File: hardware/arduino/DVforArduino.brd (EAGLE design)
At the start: 50 x 50 mm, 55 parts, among them Q1 2N7000, Q2 2N7000, U1 CML-MICRO_CMX589AE2, U2 CML-MICRO_CMX589AP4, U3 OPAMP-DUALDIP, Y1 4.9152MHz

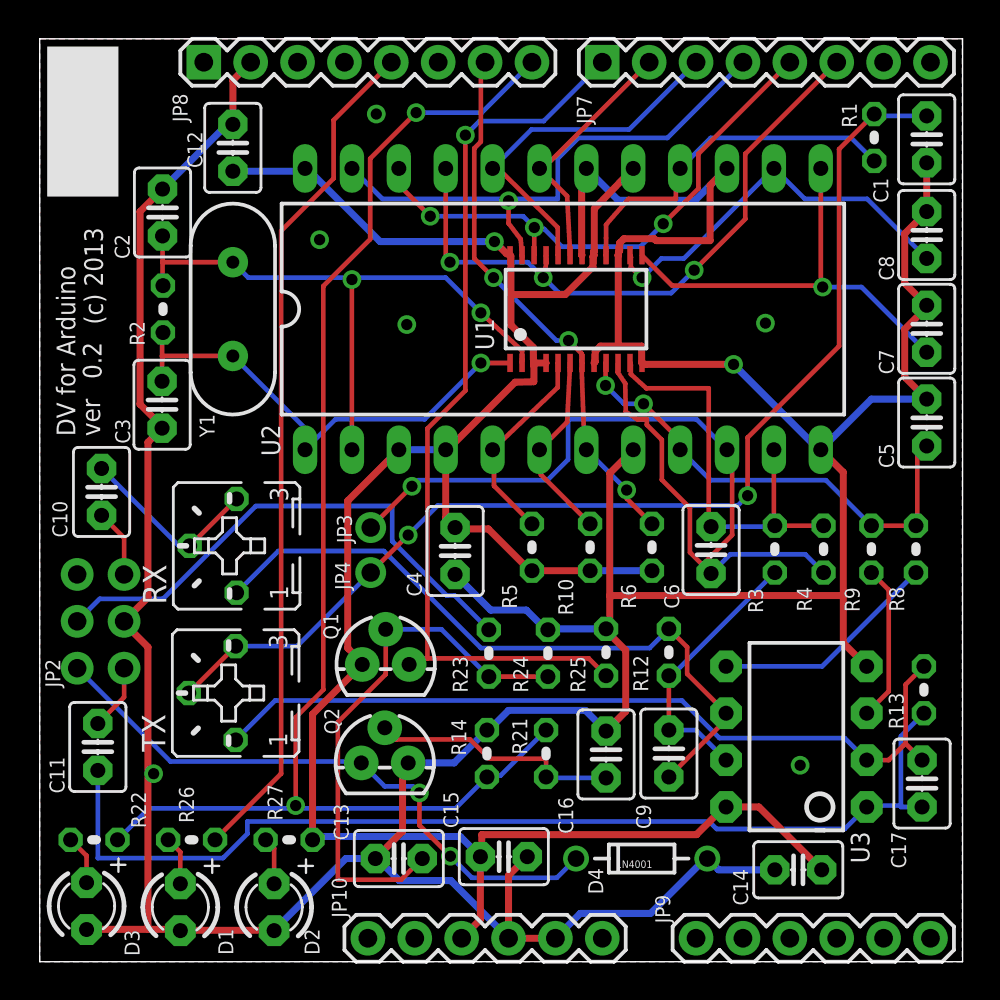
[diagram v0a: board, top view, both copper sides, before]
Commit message: 
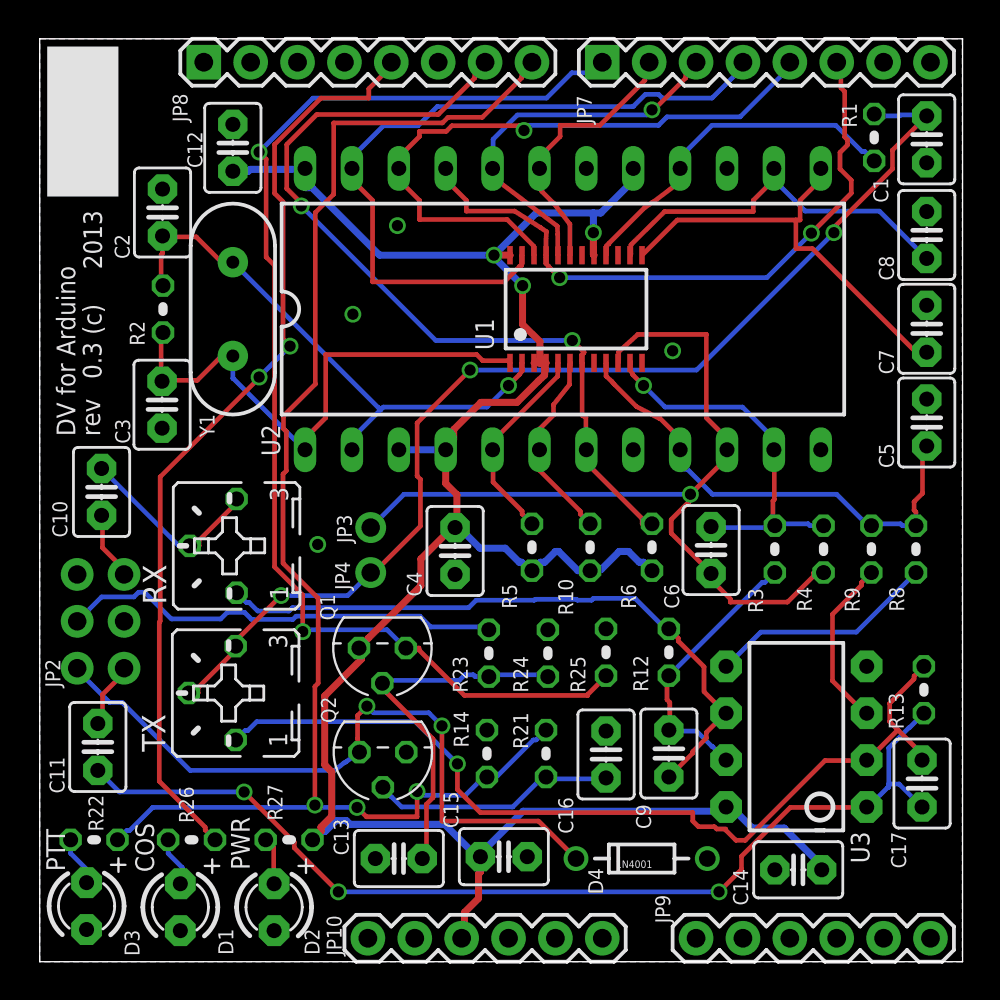
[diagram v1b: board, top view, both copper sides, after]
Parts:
- Q1, Q2: device SparkFun-DiscreteSemi:TO-92 -> transistor-fet:TO92
- moved Q1 0.91 mm to (18.6, 17.0), turned to 180 degrees
- moved Q2 0.59 mm to (18.6, 11.4), turned to 180 degrees
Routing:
- net GND: track 235.2 -> 0.00 mm, vias 7 -> 4
- net PLLACQ: track 29.6 -> 46.3 mm, vias 3 -> 2
- net COS: track 49.6 -> 66.1 mm, vias 1 -> 2
- net RX_SN: track 29.7 -> 40.1 mm, vias 1 -> 0
- net N$1: track 29.5 -> 20.1 mm
- net RADIO_PTT: track 33.2 -> 38.4 mm
- net PTT: track 73.5 -> 78.6 mm, vias 2 -> 3
- net TXCLK: track 30.2 -> 35.2 mm, vias 3 -> 1
- net RX_FB: track 52.0 -> 47.1 mm
- net COS_LED: track 46.1 -> 50.8 mm, vias 0 -> 2
- net RADIO_COS: track 28.8 -> 24.2 mm
- net N$28: track 44.7 -> 49.1 mm, vias 0 -> 1
- net XTAL: track 34.3 -> 30.3 mm, vias 2 -> 1
- net XTALN: track 26.6 -> 29.7 mm, vias 1 -> 0
- net +3V3: track 121.0 -> 123.2 mm, vias 1 -> 3
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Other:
- board text added: "0.3 (c)"
- board text added: "2013"
- board text added: "COS"
- board text added: "PTT"
- board text added: "PWR"
- board text added: "rev"
- board text removed: "(c) 2013"
- board text removed: "0.2"
- board text removed: "ver"

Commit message: 
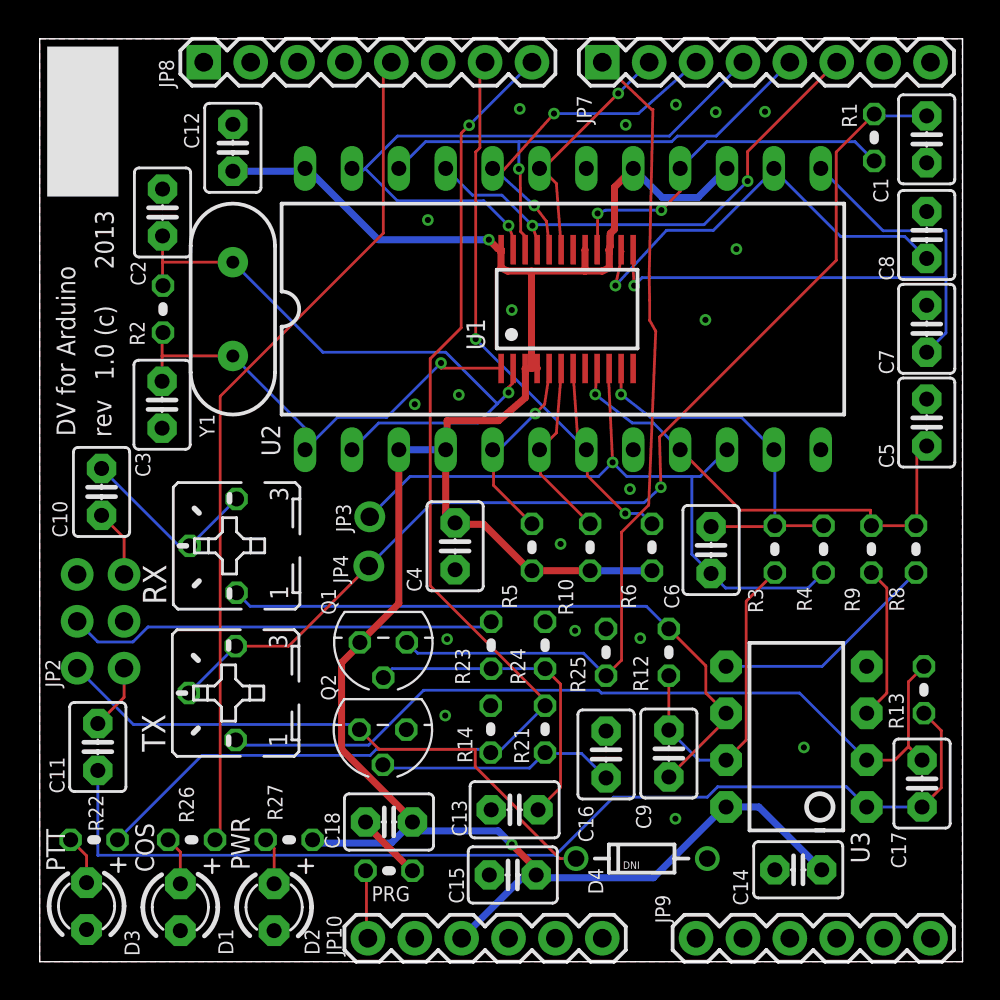
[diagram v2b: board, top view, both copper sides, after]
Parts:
- added C18: 10u, capacitor-wima:C2.5-3
- added PRG: DNI, resistor:0204V
- D4: value 1N4001 -> DNI
- U1: device 12_dollar:AIS_MK2_CML-MICRO_TSSOP24 -> mylibrary:AIS_MK2_CML-MICRO_TSSOP24
- moved C13 6.81 mm to (25.7, 8.23)
- moved R14 1.34 mm to (24.4, 12.6)
- moved R21 1.32 mm to (27.4, 12.6)
- moved Q2 1.22 mm to (18.6, 12.6)
- moved C15 1.10 mm to (25.6, 4.70), turned to 180 degrees
- moved JP3 0.59 mm to (17.9, 24.1)
- moved U1 0.48 mm to (28.6, 35.4)
- moved R24 0.46 mm to (27.4, 17.1)
- moved R23 0.45 mm to (24.5, 17.1)
- moved JP4 0.37 mm to (17.8, 21.4)
- moved Q1 0.31 mm to (18.6, 17.3)
- moved C4 0.25 mm to (22.5, 22.5)
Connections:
- new net N$6: C18.1, PRG.1
- new net RESET: JP10.1, PRG.2
- net +3V3: now also C18.2, U1.15, U2.15
- net GND: no longer U1.15, U2.15
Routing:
- net COS: track 66.1 -> 47.1 mm, vias 2 -> 0
- net PTT: track 78.6 -> 66.0 mm, vias 3 -> 1
- net PLLACQ: track 46.3 -> 34.3 mm
- net DOC1: track 23.6 -> 34.2 mm, vias 0 -> 1
- net RX_FB: track 47.1 -> 39.1 mm
- net +3V3: track 123.2 -> 130.6 mm, vias 3 -> 2
- net RXCLK: track 35.7 -> 28.4 mm
- net RADIO_PTT: track 38.4 -> 32.1 mm, vias 2 -> 0
- net RX_SN: track 40.1 -> 34.2 mm, vias 0 -> 1
- net TXCLK: track 35.2 -> 29.6 mm
- net XTAL: track 30.3 -> 35.2 mm
- net COS_LED: track 50.8 -> 46.1 mm, vias 2 -> 0
- net N$28: track 49.1 -> 45.4 mm, vias 1 -> 0
- net RESET: track 0.00 -> 3.71 mm
- net N$6: track 0.00 -> 3.71 mm
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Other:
- board text added: "1.0 (c)"
- board text removed: "0.3 (c)"
